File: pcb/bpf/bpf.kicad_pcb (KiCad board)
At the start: 2 copper layers, 58 x 53 mm, 21 parts, among them J1 input, J2 power_input, J3 audio_out, U1 TI080, U2 TI080

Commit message: finalize layout and routing
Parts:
- added C1: 1uF, Capacitor_THT:CP_Radial_D5.0mm_P2.00mm, F.Cu at (91.8, 128.0)
- added C2: 1uF, Capacitor_THT:CP_Radial_D5.0mm_P2.00mm, F.Cu at (113.8, 126.0)
- added G***: LOGO, msc-logos:msc-gears-soldermask-5mm, F.Cu at (83.2, 92.8)
- added G***: LOGO, msc-logos:msc-text-silkscreen, F.Cu at (91.2, 93.0)
- C3: renamed from C1; footprint Capacitor_THT:C_Disc_D7.5mm_W5.0mm_P7.50mm -> Capacitor_THT:C_Disc_D5.0mm_W2.5mm_P5.00mm
- C4: renamed from C2; footprint Capacitor_THT:C_Disc_D7.5mm_W5.0mm_P7.50mm -> Capacitor_THT:C_Disc_D5.0mm_W2.5mm_P5.00mm
- C5: renamed from C3; footprint Capacitor_THT:C_Disc_D7.5mm_W5.0mm_P7.50mm -> Capacitor_THT:C_Disc_D5.0mm_W2.5mm_P5.00mm
- C6: renamed from C4; footprint Capacitor_THT:C_Disc_D7.5mm_W5.0mm_P7.50mm -> Capacitor_THT:C_Disc_D5.0mm_W2.5mm_P5.00mm
- R1: value 22k ohms -> 22k
- R2, R5, R6: value 11k ohms -> 11k
- moved J3 23.1 mm to (121.2, 103.8), turned to 90 degrees
- moved H3 15.3 mm to (122.2, 94.0)
- moved H2 13.5 mm to (78.5, 94.0)
- moved J1 8.25 mm to (80.8, 103.8)
- moved R3 7.80 mm to (114.9, 117.8), turned to 0 degrees
- moved H1 7.25 mm to (122.2, 126.5)
- moved C5 6.39 mm to (91.2, 97.2)
- moved U2 5.50 mm to (99.0, 92.2)
- moved C3 5.39 mm to (85.8, 112.5), turned to 180 degrees
- moved R6 4.25 mm to (98.9, 103.5)
- moved R4 3.85 mm to (90.6, 117.8), turned to 180 degrees
- moved R5 3.20 mm to (110.5, 105.0)
- moved D1 3.10 mm to (115.0, 121.7)
- moved D2 3.05 mm to (93.1, 121.8)
- moved C6 2.91 mm to (110.5, 102.0)
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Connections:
- R4 pad 1: GND -> Net-(D2-Pad2)
- R4 pad 2: Net-(D2-Pad2) -> GND
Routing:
- net Net-(C6-Pad2): track 0.00 -> 40.8 mm
- net Net-(R2-Pad1): track 0.00 -> 20.1 mm
- net Net-(C3-Pad1): track 0.00 -> 12.5 mm
- net Net-(C5-Pad2): track 0.00 -> 10.1 mm
- net Net-(C6-Pad1): track 0.00 -> 9.10 mm
- net Net-(C3-Pad2): track 0.00 -> 9.00 mm
- net Net-(C4-Pad1): track 0.00 -> 7.29 mm
- net Net-(D2-Pad2): track 0.00 -> 4.01 mm
- net Net-(D1-Pad1): track 0.00 -> 3.97 mm
- added copper zone on F.Cu, net +5V
- added copper zone on F.Cu, net -5V
- added copper zone on B.Cu, net GND
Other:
- board size 58 x 53 mm -> 50.8 x 39.5 mm
- board text added: "+5V"
- board text added: "+5V :)"
- board text added: "-5V"
- board text added: "-5V :)"
- board text added: "BPF v1"
- board text added: "GND"
- board text added: "Optical Communication"

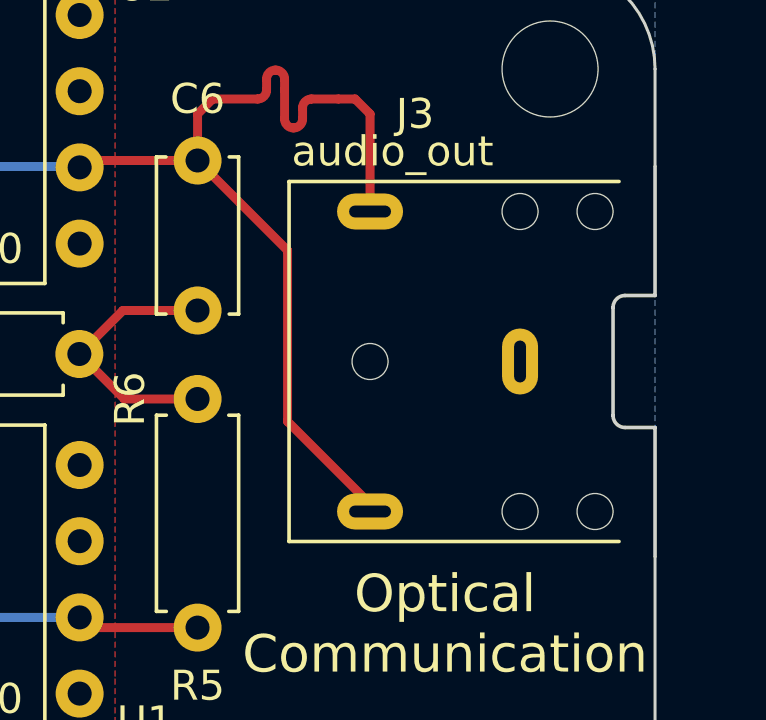
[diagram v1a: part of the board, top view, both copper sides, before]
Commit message: add silkscreen for JLC order number
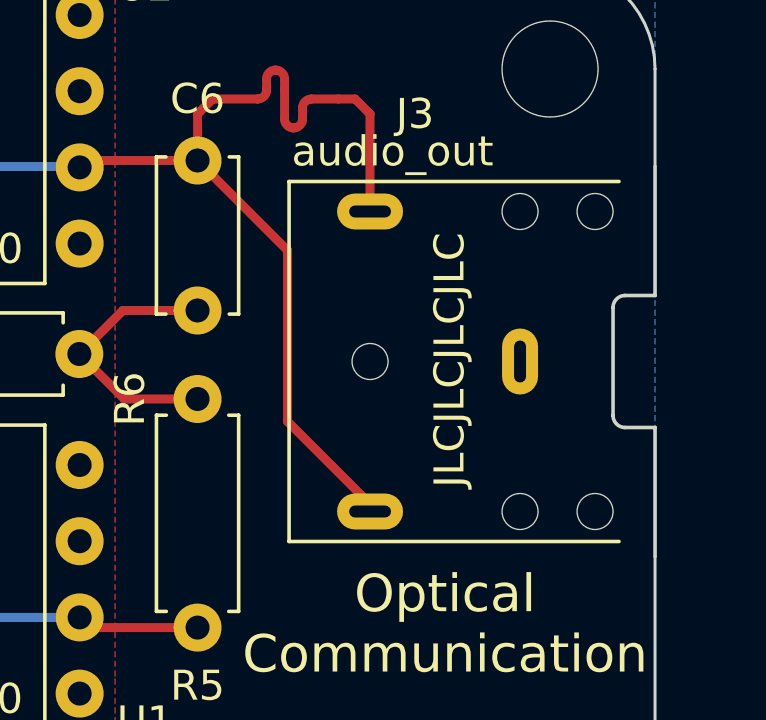
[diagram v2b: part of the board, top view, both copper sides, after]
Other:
- board text added: "JLCJLCJLCJLC"
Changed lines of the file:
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@@
     )
     (pad_to_mask_clearance 0)
+    (aux_axis_origin 75 130)
+    (grid_origin 75 130)
     (pcbplotparams
       (layerselection 0x00010fc_ffffffff)
       (disableapertmacros false)
-      (usegerberextensions false)
+      (usegerberextensions true)
       (usegerberattributes true)
-      (usegerberadvancedattributes true)
-      (creategerberjobfile true)
+      (usegerberadvancedattributes false)
+      (creategerberjobfile false)
       (svguseinch false)
       (svgprecision 6)
@@
       (psa4output false)
       (plotreference true)
-      (plotvalue true)
+      (plotvalue false)
       (plotinvisibletext false)
       (sketchpadsonfab false)
-      (subtractmaskfromsilk false)
-      (outputformat 4)
+      (subtractmaskfromsilk true)
+      (outputformat 1)
       (mirror false)
       (drillshape 0)
       (scaleselection 1)
-      (outputdirectory "")
+      (outputdirectory "gerbers")
     )
   )
@@
   (gr_line (start 122.25 90.5) (end 78.5 90.5) (layer "Edge.Cuts") (width 0.1))
   (gr_line (start 75 94) (end 75 126.5) (layer "Edge.Cuts") (width 0.1))
+  (gr_text "JLCJLCJLCJLC" (at 118.9 103.7 90) (layer "F.SilkS")
+    (effects (font (size 1 1) (thickness 0.15)))
+  )
   (gr_text "+5V :)" (at 119.25 122.5) (layer "F.SilkS")
     (effects (font (size 1.25 1.25) (thickness 0.15)))
